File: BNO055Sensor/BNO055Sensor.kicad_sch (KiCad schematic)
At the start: 8 parts, among them J1 addon_conn, U1 Adafruit_BNO055_breakout

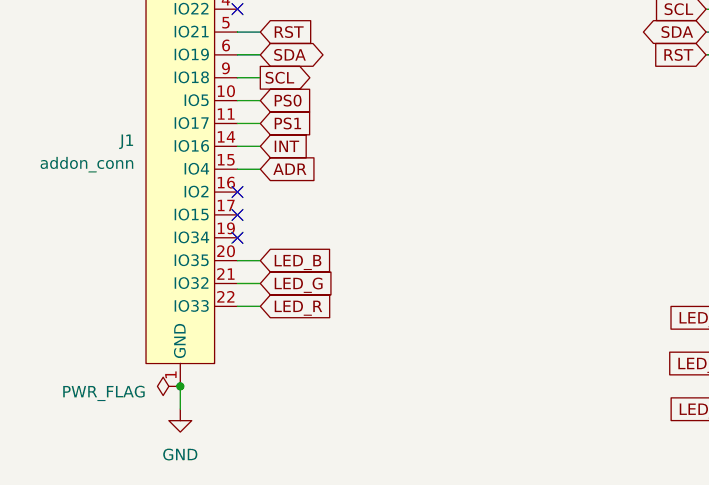
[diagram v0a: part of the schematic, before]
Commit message: Routes RGB led on sensor board
Some pin reorganization was necessary
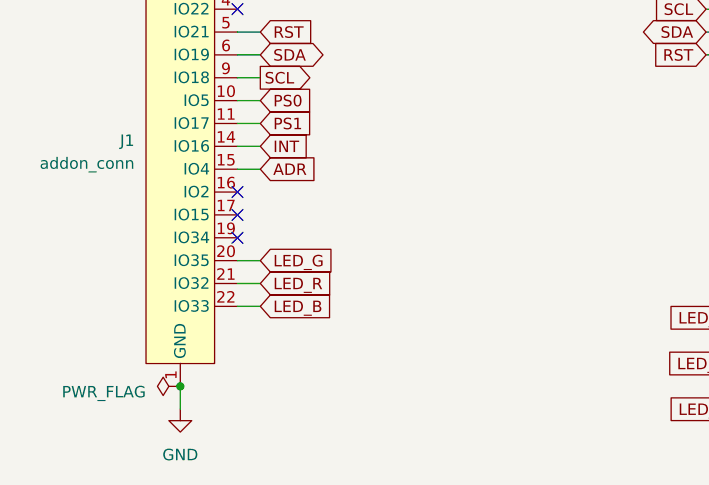
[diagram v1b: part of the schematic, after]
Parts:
- D1: footprint (none) -> GameOver:Hongzhi_Forest_HS-1204-RGB
- R1, R2, R3: footprint (none) -> Resistor_SMD:R_0805_2012Metric_Pad1.20x1.40mm_HandSolder
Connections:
- net LED_B: now also J1.22 (IO33); no longer J1.20 (IO35)
- net LED_G: now also J1.20 (IO35); no longer J1.21 (IO32)
- net LED_R: now also J1.21 (IO32); no longer J1.22 (IO33)
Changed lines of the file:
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@@
     )
   )
-  (global_label "LED_R" (shape input) (at 96.52 115.57 0) (fields_autoplaced)
+  (global_label "LED_R" (shape input) (at 96.52 113.03 0) (fields_autoplaced)
+    (effects (font (size 1.27 1.27)) (justify left))
+    (property "Intersheetrefs" "${INTERSHEET_REFS}" (id 0) (at 104.9517 113.03 0)
+      (effects (font (size 1.27 1.27)) (justify left) hide)
+    )
+  )
+  (global_label "LED_G" (shape input) (at 149.86 121.92 180) (fields_autoplaced)
+    (effects (font (size 1.27 1.27)) (justify right))
+    (property "Intersheetrefs" "${INTERSHEET_REFS}" (id 0) (at 141.4283 121.92 0)
+      (effects (font (size 1.27 1.27)) (justify right) hide)
+    )
+  )
+  (global_label "LED_B" (shape input) (at 96.52 115.57 0) (fields_autoplaced)
     (effects (font (size 1.27 1.27)) (justify left))
     (property "Intersheetrefs" "${INTERSHEET_REFS}" (id 0) (at 104.9517 115.57 0)
@@
     )
   )
-  (global_label "LED_G" (shape input) (at 149.86 121.92 180) (fields_autoplaced)
-    (effects (font (size 1.27 1.27)) (justify right))
-    (property "Intersheetrefs" "${INTERSHEET_REFS}" (id 0) (at 141.4283 121.92 0)
-      (effects (font (size 1.27 1.27)) (justify right) hide)
-    )
-  )
-  (global_label "LED_B" (shape input) (at 96.52 110.49 0) (fields_autoplaced)
+  (global_label "RST" (shape input) (at 96.52 85.09 0) (fields_autoplaced)
+    (effects (font (size 1.27 1.27)) (justify left))
+    (property "Intersheetrefs" "${INTERSHEET_REFS}" (id 0) (at 102.7141 85.09 0)
+      (effects (font (size 1.27 1.27)) (justify left) hide)
+    )
+  )
+  (global_label "INT" (shape input) (at 96.52 97.79 0) (fields_autoplaced)
+    (effects (font (size 1.27 1.27)) (justify left))
+    (property "Intersheetrefs" "${INTERSHEET_REFS}" (id 0) (at 102.1699 97.79 0)
+      (effects (font (size 1.27 1.27)) (justify left) hide)
+    )
+  )
+  (global_label "LED_R" (shape input) (at 149.86 116.84 180) (fields_autoplaced)
+    (effects (font (size 1.27 1.27)) (justify right))
+    (property "Intersheetrefs" "${INTERSHEET_REFS}" (id 0) (at 141.4283 116.84 0)
+      (effects (font (size 1.27 1.27)) (justify right) hide)
+    )
+  )
+  (global_label "LED_G" (shape input) (at 96.52 110.49 0) (fields_autoplaced)
     (effects (font (size 1.27 1.27)) (justify left))
     (property "Intersheetrefs" "${INTERSHEET_REFS}" (id 0) (at 104.9517 110.49 0)
-      (effects (font (size 1.27 1.27)) (justify left) hide)
-    )
-  )
-  (global_label "RST" (shape input) (at 96.52 85.09 0) (fields_autoplaced)
-    (effects (font (size 1.27 1.27)) (justify left))
-    (property "Intersheetrefs" "${INTERSHEET_REFS}" (id 0) (at 102.7141 85.09 0)
-      (effects (font (size 1.27 1.27)) (justify left) hide)
-    )
-  )
-  (global_label "INT" (shape input) (at 96.52 97.79 0) (fields_autoplaced)
-    (effects (font (size 1.27 1.27)) (justify left))
-    (property "Intersheetrefs" "${INTERSHEET_REFS}" (id 0) (at 102.1699 97.79 0)
-      (effects (font (size 1.27 1.27)) (justify left) hide)
-    )
-  )
-  (global_label "LED_R" (shape input) (at 149.86 116.84 180) (fields_autoplaced)
-    (effects (font (size 1.27 1.27)) (justify right))
-    (property "Intersheetrefs" "${INTERSHEET_REFS}" (id 0) (at 141.4283 116.84 0)
-      (effects (font (size 1.27 1.27)) (justify right) hide)
-    )
-  )
-  (global_label "LED_G" (shape input) (at 96.52 113.03 0) (fields_autoplaced)
-    (effects (font (size 1.27 1.27)) (justify left))
-    (property "Intersheetrefs" "${INTERSHEET_REFS}" (id 0) (at 104.9517 113.03 0)
       (effects (font (size 1.27 1.27)) (justify left) hide)
     )
@@
       (effects (font (size 1.27 1.27)))
     )
-    (property "Footprint" "" (id 2) (at 157.48 127 0)
+    (property "Footprint" "Resistor_SMD:R_0805_2012Metric_Pad1.20x1.40mm_HandSolder" (id 2) (at 157.48 127 0)
       (effects (font (size 1.27 1.27)) hide)
     )
@@
       (effects (font (size 1.27 1.27)))
     )
-    (property "Footprint" "" (id 2) (at 157.48 121.92 0)
+    (property "Footprint" "Resistor_SMD:R_0805_2012Metric_Pad1.20x1.40mm_HandSolder" (id 2) (at 157.48 121.92 0)
       (effects (font (size 1.27 1.27)) hide)
     )
@@
       (effects (font (size 1.27 1.27)))
     )
-    (property "Footprint" "" (id 2) (at 172.72 123.19 0)
+    (property "Footprint" "GameOver:Hongzhi_Forest_HS-1204-RGB" (id 2) (at 172.72 123.19 0)
       (effects (font (size 1.27 1.27)) hide)
     )
@@
       (effects (font (size 1.27 1.27)))
     )
-    (property "Footprint" "" (id 2) (at 157.48 116.84 0)
-      (effects (font (size 1.27 1.27)) hide)
-    )
+    (property "Footprint" "Resistor_SMD:R_0805_2012Metric_Pad1.20x1.40mm_HandSolder" (id 2) (at 157.48 116.84 0)
+      (effects (font (size 1.27 1.27)) hide)
+    )

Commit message: Adds logo and revision number to sensor board
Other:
- title: Game Over addon -> Game Over Sensor addon
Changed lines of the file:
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@@
   (paper "A4")
   (title_block
-    (title "Game Over addon")
+    (title "Game Over Sensor addon")
     (rev "0.1")
     (company "Flávio Amieiro")

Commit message: Updates BNO055Sensor board after changes in the addon connector
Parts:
- removed D1: LED_RGBA, GameOver:Hongzhi_Forest_HS-1204-RGB, symbol Device:LED_RGBA
- added D1: LED_BGAR, GameOver:Hongzhi_Forest_HS-1204-RGB, symbol Device:LED_BGAR
- J1: footprint GameOver:TXGA_FFC05036-24SBD113W5M_1x24_P0.50mm_Horizontal -> GameOver:Addon_conn_TXGA_FFC05036-24SBD113W5M_1x24_P0.50mm_Horizontal
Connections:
- net +3V3: now also D1.3 (A); no longer J1.8 (3v3)
- net GND: no longer J1.18 (GND), J1.7 (GND)
- net LED_G: now also J1.21 (IO2); no longer J1.20 (IO35)
- net LED_R: now also J1.20 (IO27); no longer J1.21 (IO32)
- net SCL: now also J1.8 (IO18); no longer J1.9 (IO18)
- net at R3.2: now also D1.1 (BK)
- net at R2.2: now also D1.2 (GK)
- net at R1.2: now also D1.4 (RK)
- no-connect marks 6 -> 9

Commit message: Adds logo to BNO055 sensor board schematics
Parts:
- added LOGO1: GameOver_logo, symbol GameOver:GameOver_logo
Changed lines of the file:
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@@
     (pin "1")
+  )
+  (symbol (lib_id "GameOver:GameOver_logo") (at 227.33 120.65 0) (unit 1)
+    (in_bom no) (on_board yes)
+    (property "Reference" "LOGO1" (id 0) (at 224.155 115.57 0)
+      (effects (font (size 1.27 1.27)) (justify left))
+    )
+    (property "Value" "GameOver_logo" (id 1) (at 227.33 127 0)
+      (effects (font (size 1.27 1.27)) hide)
+    )
+    (property "Footprint" "" (id 2) (at 227.33 120.65 0)
+      (effects (font (size 1.27 1.27)) hide)
+    )
+    (property "Datasheet" "" (id 3) (at 227.33 120.65 0)
+      (effects (font (size 1.27 1.27)) hide)
+    )
   )
   (symbol (lib_id "Device:R_Small_US") (at 157.48 121.92 90) (unit 1)
@@
       (reference "J1") (unit 1) (value "addon_conn") (footprint "GameOver:Addon_conn_TXGA_FFC05036-24SBD113W5M_1x24_P0.50mm_Horizontal")
     )
+    (path "/5a8b9a29-2bd9-4845-a603-2ff6b9184494"
+      (reference "LOGO1") (unit 1) (value "GameOver_logo") (footprint "GameOver:logo_fcu")
+    )
     (path "/df729cdb-2037-48dc-ae33-70081f93ee69"

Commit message: Updates logo in sensor board schematics
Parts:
- LOGO1: footprint (none) -> GameOver:logo_fcu
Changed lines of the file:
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@@
       (effects (font (size 1.27 1.27)) hide)
     )
-    (property "Footprint" "" (id 2) (at 227.33 120.65 0)
+    (property "Footprint" "GameOver:logo_fcu" (id 2) (at 227.33 120.65 0)
       (effects (font (size 1.27 1.27)) hide)
     )

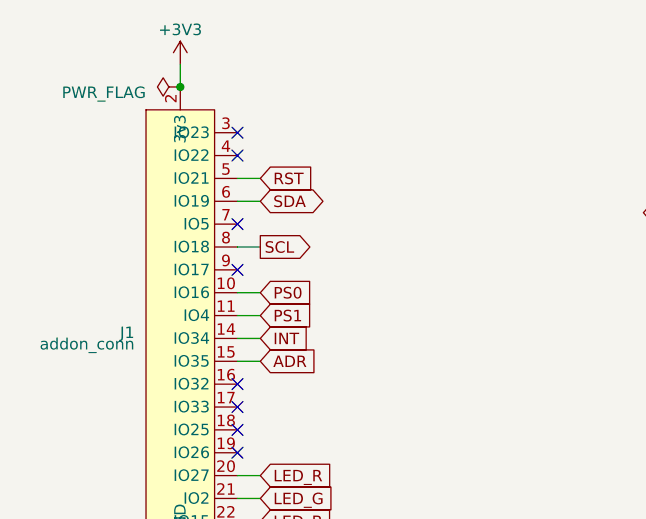
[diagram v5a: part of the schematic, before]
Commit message: Updates all add-on boards with fix introduced in 692041
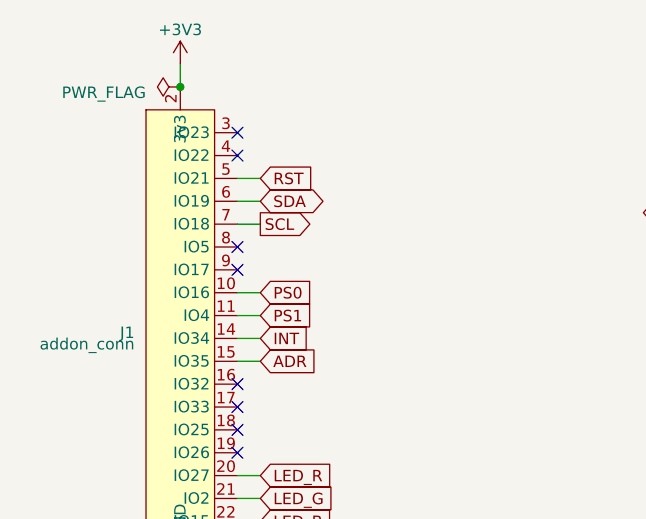
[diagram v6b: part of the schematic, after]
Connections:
- net SCL: now also J1.7 (IO18); no longer J1.8 (IO18)
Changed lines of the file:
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@@
   )
   (no_connect (at 160.02 74.93))
-  (no_connect (at 93.98 86.36))
+  (no_connect (at 93.98 88.9))
   (no_connect (at 93.98 111.76))
   (no_connect (at 93.98 109.22))
@@
     (stroke (width 0) (type default))
   )
-  (wire (pts (xy 93.98 88.9) (xy 96.52 88.9))
+  (wire (pts (xy 93.98 86.36) (xy 96.52 86.36))
     (stroke (width 0) (type default))
   )
@@
     )
   )
-  (global_label "SCL" (shape output) (at 96.52 88.9 0) (fields_autoplaced)
-    (effects (font (size 1.27 1.27)) (justify left))
-    (property "Intersheetrefs" "${INTERSHEET_REFS}" (id 0) (at 102.7746 88.9 0)
-      (effects (font (size 1.27 1.27)) (justify left) hide)
-    )
+  (global_label "SCL" (shape output) (at 96.52 86.36 0) (fields_autoplaced)
+    (effects (font (size 1.27 1.27)) (justify left))
+    (property "Intersheetrefs" "${INTERSHEET_REFS}" (id 0) (at 102.7746 86.36 0)
+      (effects (font (size 1.27 1.27)) (justify left) hide)
+    )

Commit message: Updates all schematic PDFs to version 1.0
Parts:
- ?: renamed from R3; value 1kΩ -> (none); footprint Resistor_SMD:R_0805_2012Metric_Pad1.20x1.40mm_HandSolder -> (none)
- ?: renamed from H2; value ~ -> (none); footprint MountingHole:MountingHole_2.2mm_M2_Pad_Via -> (none)
- ?: renamed from LOGO1; value GameOver_logo -> (none); footprint GameOver:logo_fcu -> (none)
- ?: renamed from R2; value 1kΩ -> (none); footprint Resistor_SMD:R_0805_2012Metric_Pad1.20x1.40mm_HandSolder -> (none)
- ?: renamed from H1; value ~ -> (none); footprint MountingHole:MountingHole_2.2mm_M2_Pad_Via -> (none)
- ?: renamed from U1; value Adafruit_BNO055_breakout -> (none); footprint GameOver:Adafruit_BNO055_breakout -> (none)
- ?: renamed from J1; value addon_conn -> (none); footprint GameOver:Addon_conn_TXGA_FFC05036-24SBD113W5M_1x24_P0.50mm_Horizontal -> (none)
- ?: renamed from R1; value 1kΩ -> (none); footprint Resistor_SMD:R_0805_2012Metric_Pad1.20x1.40mm_HandSolder -> (none)
- ?: renamed from D1; value LED_BGAR -> (none); footprint GameOver:Hongzhi_Forest_HS-1204-RGB -> (none)
